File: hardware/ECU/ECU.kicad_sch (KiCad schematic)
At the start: 75 parts, among them IC1 IR4427SPBF, IC2 EL357NB_TA_-G, IC3 EL357NB_TA_-G, J1 USB_B_Micro, J2 TFP09-2-12B, J3 Connector, Q1 S8050, Q2 S8050, Q3 RJP63K2, Q4 RJP63K2, SW1 RESET, SW2 EN, U1 AMS1117-3.3, U2 AMS1117-3.3, U3 CP2102N-Axx-xQFN28, U4 ESP32-WROOM-32U

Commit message: backup
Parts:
- removed C15: 22u, Capacitor_SMD:C_0603_1608Metric_Pad1.08x0.95mm_HandSolder, symbol Device:C
- removed C21, C22, C23: 1n, Capacitor_SMD:C_0603_1608Metric_Pad1.08x0.95mm_HandSolder, symbol Device:C
- removed C8: 22u, Capacitor_SMD:C_0805_2012Metric_Pad1.18x1.45mm_HandSolder, symbol Device:C
- removed C9: 100n, Capacitor_SMD:C_0603_1608Metric_Pad1.08x0.95mm_HandSolder, symbol Device:C
- removed D10: 1n4007, Diode_SMD:D_SMA, symbol Device:D
- removed D11, D3, D8: LED, LED_SMD:LED_0603_1608Metric_Pad1.05x0.95mm_HandSolder, symbol Device:LED
- removed D4: 3.6v, Diode_SMD:D_1206_3216Metric_Pad1.42x1.75mm_HandSolder, symbol Device:D_Zener
- removed D5: 1n4001, Diode_SMD:D_SMA, symbol Device:D
- removed D6, D7: 5v, Diode_SMD:D_SOD-523, symbol Device:D_Zener
- removed J1: USB_B_Micro, Connector_USB:USB_Micro-B_Molex-105017-0001, symbol Connector:USB_B_Micro
- removed J3: Connector, Connector_PinHeader_2.54mm:PinHeader_2x06_P2.54mm_Vertical, symbol Connector:Conn_01x12_Pin
- removed Q1, Q2: S8050, Package_TO_SOT_SMD:SOT-23, symbol Transistor_BJT:S8050
- removed U1: AMS1117-3.3, Package_TO_SOT_SMD:SOT-223-3_TabPin2, symbol Regulator_Linear:AMS1117-3.3
- removed U3: CP2102N-Axx-xQFN28, Package_DFN_QFN:QFN-28-1EP_5x5mm_P0.5mm_EP3.35x3.35mm, symbol Interface_USB:CP2102N-Axx-xQFN28
- removed U4: ESP32-WROOM-32U, RF_Module:ESP32-WROOM-32U, symbol RF_Module:ESP32-WROOM-32U
- added C8: 100u, Capacitor_SMD:CP_Elec_10x10, symbol Device:C_Polarized
- added C9: 1n, Capacitor_SMD:CP_Elec_10x10, symbol Device:C_Polarized
- added D3, D6: ss36, Diode_SMD:D_SMC, symbol Device:D_Schottky
- added D4: m7, Diode_SMD:D_SMA, symbol Device:D
- added D5: LED, LED_SMD:LED_0603_1608Metric_Pad1.05x0.95mm_HandSolder, symbol Device:LED
- added IC4: ESP32-S3-WROOM-1U-N8R8, ESP32S3WROOM1UN8R8, symbol My_Library:ESP32-S3-WROOM-1U-N8R8
- added JP1: BOOT, Connector_PinHeader_2.54mm:PinHeader_1x02_P2.54mm_Vertical, symbol Jumper:Jumper_2_Open
- added JP2: ADDR, Connector_PinHeader_2.54mm:PinHeader_1x03_P2.54mm_Vertical, symbol Jumper:Jumper_3_Open
- added L1: 100u, My_Lirbrary:INDPM102100X400N, symbol Device:L
- added R26, R32, R34, R35, R36, R37: 10k, Resistor_SMD:R_0603_1608Metric_Pad0.98x0.95mm_HandSolder, symbol Device:R
- added R27, R28, R29, R30, R31: 1k, Resistor_SMD:R_0603_1608Metric_Pad0.98x0.95mm_HandSolder, symbol Device:R
- added R33: 100, Resistor_SMD:R_0603_1608Metric_Pad0.98x0.95mm_HandSolder, symbol Device:R
- added U1: LM2576S-5, Package_TO_SOT_SMD:TO-263-5_TabPin3, symbol Regulator_Switching:LM2576S-5
- added U3: LM75A, symbol Sensor_Temperature:LM75B
- added U4: ADS1115IDGS, Package_SO:TSSOP-10_3x3mm_P0.5mm, symbol Analog_ADC:ADS1115IDGS
- C10: value 10u -> 100n; footprint Capacitor_SMD:C_0603_1608Metric_Pad1.08x0.95mm_HandSolder -> Capacitor_SMD:C_0805_2012Metric_Pad1.18x1.45mm_HandSolder
- C11, C14: footprint Capacitor_SMD:C_0603_1608Metric_Pad1.08x0.95mm_HandSolder -> Capacitor_SMD:C_0603_1608Metric
- C12: value 10u -> 100n; footprint Capacitor_SMD:C_0603_1608Metric_Pad1.08x0.95mm_HandSolder -> Capacitor_SMD:C_0603_1608Metric
- C13: value 1n -> 100n; footprint Capacitor_SMD:C_0603_1608Metric_Pad1.08x0.95mm_HandSolder -> Capacitor_SMD:C_0603_1608Metric
- C3, C4: footprint Capacitor_SMD:C_0805_2012Metric_Pad1.18x1.45mm_HandSolder -> Capacitor_SMD:C_0603_1608Metric
- C5: value 100n -> 1u; footprint Capacitor_SMD:C_0805_2012Metric_Pad1.18x1.45mm_HandSolder -> Capacitor_SMD:C_0603_1608Metric
- R1: value 1M -> 10k
- R22, R23: value 470 -> 10k
- R24: value 5k -> 10k
- R25: value 1k -> 10k
- R3, R9: value 2k -> 10k
- R4, R5, R8: value 12k -> 10k
- R6, R7: value 0 -> 10k
- SW1: value RESET -> RESET BTN; footprint Button_Switch_SMD:SW_Push_1P1T_NO_CK_KMR2 -> Button_Switch_SMD:SW_SPST_PTS810
- SW2: value EN -> ZERO BTN; footprint Button_Switch_SMD:SW_Push_1P1T_NO_CK_KMR2 -> Button_Switch_SMD:SW_SPST_PTS810
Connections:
- net RXD is gone; now on net +3.3V: R6.2
- net TXD is gone; now on net +3.3V: R7.2
- net VBUS is gone; now on net GND: C10.1, C3.1, C4.1, R3.1
- net +12V: now also C8.1, U1.1 (VIN); no longer C2.1, C7.1, R2.1, U2.3 (VI)
- net +3.3V: now also C10.2, C13.2, C3.2, C4.2, R23.1, R24.1, R25.2, R4.2, R5.2, IC4.2 (3V3), JP2.1 (A), R26.2, R29.2, R30.2, R32.1, R34.1, R36.1, R37.1, U3.8 (+Vs), U4.8 (VDD); no longer C11.1, C12.1, C14.2, C5.1, R24.2, R8.2
- net COIL_PIN: now also IC2.1 (A), IC4.38 (IO2); no longer IC3.1 (A)
- net FUEL: now also D6.1 (K)
- net FUEL_PIN: now also IC3.1 (A), IC4.39 (IO1); no longer IC2.1 (A)
- net GND: now also C11.1, C12.1, C13.1, C5.1, R1.1, R22.2, R8.1, C8.2, C9.2, D3.2 (A), D6.2 (A), IC4.1 (GND_1), IC4.40 (GND_2), IC4.41 (GND_3), IC4.42 (GND_4), IC4.43 (GND_5), IC4.44 (GND_6), IC4.45 (GND_7), IC4.46 (GND_8), IC4.47 (GND_9), IC4.48 (GND_10), IC4.49 (GND_11), JP1.2 (B), JP2.3 (B), R31.1, U1.3 (GND), U1.5 (~{ON}/OFF), U3.4 (GND), U4.3 (GND); no longer C10.2, C11.2, C12.2, C13.2, C3.2, C4.2, C5.2, R1.2, R25.1
- net O2: now also R33.1
- net at R3.2: now also IC1.4 (INB), IC3.3 (E)
- net at R22.1: now also IC4.16 (IO46); no longer SW1.2
- net at R7.1: now also IC4.15 (IO3)
- net SCL_0: now reaches R5.1
- net SCL_0: now also IC4.7 (IO7), U4.10 (SCL)
- net at R9.2: now also U3.5 (A2)
- net at SW2.2: now also C12.2, R28.2; no longer R23.1
- net at IC1.2 (INA), IC2.3 (E): now also R1.2
- net RESET_PIN: now reaches R6.1
- net RESET_PIN: now also C5.2, IC4.3 (EN), R27.1, R29.1
- net SDA_0: now reaches R4.1
- net SDA_0: now also IC4.6 (IO6), U4.9 (SDA)
- net COIL_IGBT: no longer names the net of IC1.5 (OUT_B)
- net COIL_IGBT: now also R15.2; no longer R11.2
- removed net EN: C13.1, R23.2, R8.1
- net FUEL_IGBT: no longer names the net of IC1.7 (OUT_A)
- net FUEL_IGBT: now also R11.2; no longer R15.2
- removed net IO0: R22.2, R24.1
- new net: D3.1 (K), L1.1, U1.2 (OUT)
- new net: C9.1, D4.2 (A), L1.2, U1.4 (FB)
- new net: IC4.26 (IO45), R8.2
- new net: IC4.27 (IO0), JP1.1 (A)
- new net: R35.1, U4.1 (ADDR)
- new net: JP2.2 (C), R35.2
- new net: R37.2, U4.6 (AIN2)
- new net: C11.2, R27.2, SW1.2
- new net: R23.2, U3.6 (A1)
- new net: D5.1 (K), R31.2
- new net: R24.2, U3.7 (A0)
- new net: R36.2, U4.5 (AIN1)
- new net: C14.2, R33.2, U4.7 (AIN3)
- new net: R34.2, U4.4 (AIN0)
- new net: R32.2, U4.2 (ALERT/RDY)
- new net +5V: C2.1, C7.1, D4.1 (K), R2.1, U2.3 (VI)
- new net CAPTURE_PIN: IC4.10 (IO17)
- new net FSPI_CLK: IC4.20 (IO12)
- new net FSPI_CS: IC4.18 (IO10)
- new net FSPI_MISO: IC4.21 (IO13)
- new net FSPI_MOSI: IC4.19 (IO11)
- new net FUEL_PUMP_PIN: IC4.31 (IO38)
- new net LED_PIN: D5.2 (A), IC4.9 (IO16)
- new net O2_HEATER_PIN: IC4.30 (IO37)
- new net SCL_1: IC4.17 (IO9), R26.1, U3.2 (SCL)
- new net SDA_1: IC4.12 (IO8), R25.1, U3.1 (SDA)
- new net USB_D+: IC4.14 (IO20)
- new net USB_D-: IC4.13 (IO19)
- new net ZERO_PIN: IC4.11 (IO18), R28.1, R30.1
- no-connect marks 42 -> 22
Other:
- note added: "Control"
- note added: "ECU Temp Sensor"
- note added: "MCU"
- note added: "O2_READER"
- note added: "POWER REGULATION"
- note removed: "Battery Regulator"
- note removed: "Buttons"
- note removed: "Connector"
- note removed: "ESP32"
- note removed: "GATE DRIVER"
- note removed: "Power LED"
- note removed: "USB Regulator"
- note removed: "USB to UART"
- moved on the sheet: C1, C16, C17, C18, C19, C2, C20, C6, C7, D1, D2, D9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

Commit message: ECU hardware v0.2 candidate
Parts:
- removed D4: m7, Diode_SMD:D_SMA, symbol Device:D
- removed JP2: ADDR, Connector_PinHeader_2.54mm:PinHeader_1x03_P2.54mm_Vertical, symbol Jumper:Jumper_3_Open
- removed R29: 1k, Resistor_SMD:R_0603_1608Metric_Pad0.98x0.95mm_HandSolder, symbol Device:R
- removed U3: LM75A, symbol Sensor_Temperature:LM75B
- added C21, C24, C25, C26, C27, C28, C29: 100n, Capacitor_SMD:C_0603_1608Metric, symbol Device:C
- added D10, D7: m7, Diode_SMD:D_SMA, symbol Device:D
- added D4: 5v, Diode_SMD:D_1206_3216Metric_Pad1.42x1.75mm_HandSolder, symbol Device:D_Zener
- added D8: ss36, Diode_SMD:D_SMC, symbol Device:D_Schottky
- added IC5: EL357NB_TA_-G, MyLibrary:EL357NG, symbol My_Library:EL357NB_TA_-G
- added J1: AQS, Connector_JST:JST_XH_B6B-XH-A_1x06_P2.50mm_Vertical, symbol Connector:Conn_01x06_Pin
- added J3: CAM_SENSOR, Connector_JST:JST_XH_B6B-XH-A_1x06_P2.50mm_Vertical, symbol Connector:Conn_01x06_Pin
- added J4: USB_B, Connector_USB:USB_B_TE_5787834_Vertical, symbol Connector:USB_B
- added J5: BATTERY, Connector_Molex:Molex_KK-396_5273-02A_1x02_P3.96mm_Vertical, symbol Connector:Conn_01x02_Pin
- added J6: GATEs, Connector_Molex:Molex_KK-396_5273-06A_1x06_P3.96mm_Vertical, symbol Connector:Conn_01x06_Pin
- added J8: CAPTURE_TRG, Connector_JST:JST_XH_B2B-XH-A_1x02_P2.50mm_Vertical, symbol Connector:Conn_01x02_Pin
- added Q1: RJP63K2, Package_TO_SOT_SMD:TO-263-2, symbol Device:Q_NIGBT_GCE
- added R38: 0, Resistor_SMD:R_0603_1608Metric_Pad0.98x0.95mm_HandSolder, symbol Device:R
- added R39: 100, Resistor_SMD:R_0603_1608Metric_Pad0.98x0.95mm_HandSolder, symbol Device:R
- added R42, R43, R51: 10k, Resistor_SMD:R_0603_1608Metric_Pad0.98x0.95mm_HandSolder, symbol Device:R
- added R45: 0.01, MyLibrary:RESC10052X106N, symbol Device:R
- added R47: 130k, Resistor_SMD:R_0603_1608Metric_Pad0.98x0.95mm_HandSolder, symbol Device:R
- added R50: 5.6k, Resistor_SMD:R_0603_1608Metric_Pad0.98x0.95mm_HandSolder, symbol Device:R
- added R52, R53, R54: 1k, Resistor_SMD:R_0603_1608Metric_Pad0.98x0.95mm_HandSolder, symbol Device:R
- added U5: ADS1115IDGS, Package_SO:TSSOP-10_3x3mm_P0.5mm, symbol Analog_ADC:ADS1115IDGS
- added U6: INA180A3, Package_TO_SOT_SMD:SOT-23-5, symbol Amplifier_Current:INA180A3
- added U7: SRV05-4, Package_TO_SOT_SMD:SOT-23-6, symbol Power_Protection:SRV05-4
- C10: footprint Capacitor_SMD:C_0805_2012Metric_Pad1.18x1.45mm_HandSolder -> Capacitor_SMD:C_0603_1608Metric
- IC1: footprint My_Lirbrary:SOIC127P600X175-8N -> MyLibrary:SOIC127P600X175-8N
- IC2, IC3: footprint SOP254P700X200-4N -> MyLibrary:EL357NG
- IC4: footprint ESP32S3WROOM1UN8R8 -> MyLibrary:ESP32S3WROOM1UN4
- J2: footprint TFP09212B -> MyLibrary:TFP09212B
- L1: footprint My_Lirbrary:INDPM102100X400N -> MyLibrary:INDPM102100X400N
- R16, R17, R18, R19, R20, R21: footprint Resistor_SMD:R_0603_1608Metric_Pad0.98x0.95mm_HandSolder -> Resistor_SMD:R_0603_1608Metric
- R27, R28: value 1k -> 100
- R34, R36, R37, R9: value 10k -> 100
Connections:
- net +3.3V: now also R21.1, R24.2, R4.1, R5.1, C21.2, R43.1, R51.2, R53.2, U5.8 (VDD), U6.5 (V+); no longer R21.2, R23.1, R24.1, R34.1, R36.1, R37.1, R4.2, R5.2, R9.1
- net +5V: now also C9.1, L1.2, U1.4 (FB), D10.2 (A), J1.6 (Pin_6), J3.6 (Pin_6), R54.2; no longer C2.1, C7.1, R2.1, U2.3 (VI)
- net CAPTURE_PIN: now also IC4.24 (IO47), R52.1, R53.1; no longer IC4.10 (IO17)
- net COIL: now also J6.1 (Pin_1)
- net COIL_PIN: now also IC4.4 (IO4); no longer IC4.38 (IO2)
- net FSPI_CLK: now also J3.4 (Pin_4)
- net FSPI_CS: now also J3.2 (Pin_2)
- net FSPI_MISO: now also J3.5 (Pin_5)
- net FSPI_MOSI: now also J3.3 (Pin_3)
- net FUEL: now also D6.2 (A), J6.3 (Pin_3); no longer D6.1 (K)
- net FUEL_PIN: now also IC4.5 (IO5); no longer IC4.39 (IO1)
- net FUEL_PUMP_PIN: now also IC4.6 (IO6), IC5.1 (A); no longer IC4.31 (IO38)
- net GND: now also R23.1, R35.1, R9.1, C21.1, C24.1, C25.1, C26.1, C27.1, C28.1, C29.1, D4.2 (A), J1.1 (Pin_1), J3.1 (Pin_1), J4.4 (GND), J4.5 (Shield), J8.2 (Pin_2), Q1.3 (E), R42.1, R45.1, R50.1, U5.3 (GND), U6.2 (GND), U6.3 (+), U7.2 (VN); no longer D6.2 (A)
- net LED_PIN: now also IC4.25 (IO48); no longer IC4.9 (IO16)
- net SCL_0: now also IC4.8 (IO15), R26.1; no longer IC4.7 (IO7), R5.1
- net SCL_1: now also IC4.38 (IO2), R4.2, U5.10 (SCL); no longer IC4.17 (IO9), R26.1
- net SDA_0: now also IC4.7 (IO7), R25.1; no longer IC4.6 (IO6), R4.1
- net SDA_1: now also IC4.39 (IO1), R5.2, U5.9 (SDA); no longer IC4.12 (IO8), R25.1
- net SD_CLK: now also IC4.34 (IO41)
- net SD_CMD: now also IC4.35 (IO42)
- net SD_DAT0: now also IC4.33 (IO40)
- net USB_D+: now also J4.3 (D+), U7.3 (IO2), U7.4 (IO3)
- net USB_D-: now also J4.2 (D-), U7.1 (IO1), U7.6 (IO4)
- net ZERO_PIN: now also IC4.9 (IO16); no longer IC4.11 (IO18)
- net at R9.2: now also IC5.2 (K)
- net SD_DAT1: now reaches IC4.32 (IO39)
- net SD_DAT1: now also J2.8 (DAT1), R21.2
- net SD_DAT3: now reaches IC4.36 (RXD0)
- net SD_DAT3: now also J2.2 (CD/DAT3), R19.2
- net SD_DAT2: now reaches IC4.37 (TXD0)
- net SD_DAT2: now also J2.1 (DAT2), R20.2
- net at U4.1 (ADDR): now also R35.2; no longer R35.1
- net at R37.2, U4.6 (AIN2): now also C27.2
- net at R23.2: now also IC5.3 (E), R38.2
- net at R36.2, U4.5 (AIN1): now also C28.2
- net at R34.2, U4.4 (AIN0): now also C29.2
- net +12V renamed +BATT
- net +BATT: now also D6.1 (K), D8.1 (K), IC5.4 (C), J5.2 (Pin_2), J6.2 (Pin_2), J6.4 (Pin_4), J6.6 (Pin_6), R47.2
- net O2 renamed AFR
- net AFR: now also J1.5 (Pin_5)
- net O2_HEATER_PIN: no longer names the net of IC4.30 (IO37)
- new net: C25.2, R47.1, R50.2, U5.4 (AIN0)
- new net: C24.2, R39.2, U5.5 (AIN1)
- new net: D7.2 (A), J4.1 (VBUS), U7.5 (VP)
- new net: R24.1, U5.6 (AIN2)
- new net: R43.2, U5.2 (ALERT/RDY)
- new net: C26.2, J8.1 (Pin_1), R52.2
- new net: Q1.1 (G), R38.1
- new net: R42.2, U5.1 (ADDR)
- new net: R51.1, U5.7 (AIN3)
- new net +4V: C2.1, C7.1, D10.1 (K), D4.1 (K), D7.1 (K), R2.1, U2.3 (VI)
- new net -BATT: J5.1 (Pin_1), R45.2, U6.4 (-)
- new net BATT_OUT: R39.1, U6.1
- new net IAT: J1.2 (Pin_2), R34.1, R54.1
- new net MPS: J1.3 (Pin_3), R36.1
- new net PUMP: D8.2 (A), J6.5 (Pin_5), Q1.2 (C)
- new net TPS: J1.4 (Pin_4), R37.1
- no-connect marks 22 -> 14
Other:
- note added: "Air Quality Sensor"
- note added: "Connectors"
- note added: "Power Sense(s)"
- note removed: "ECU Temp Sensor"
- note removed: "O2_READER"
- moved on the sheet: C1, C11, C12, C13, C14, C16, C2, C3, C4, C5, C6, C7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

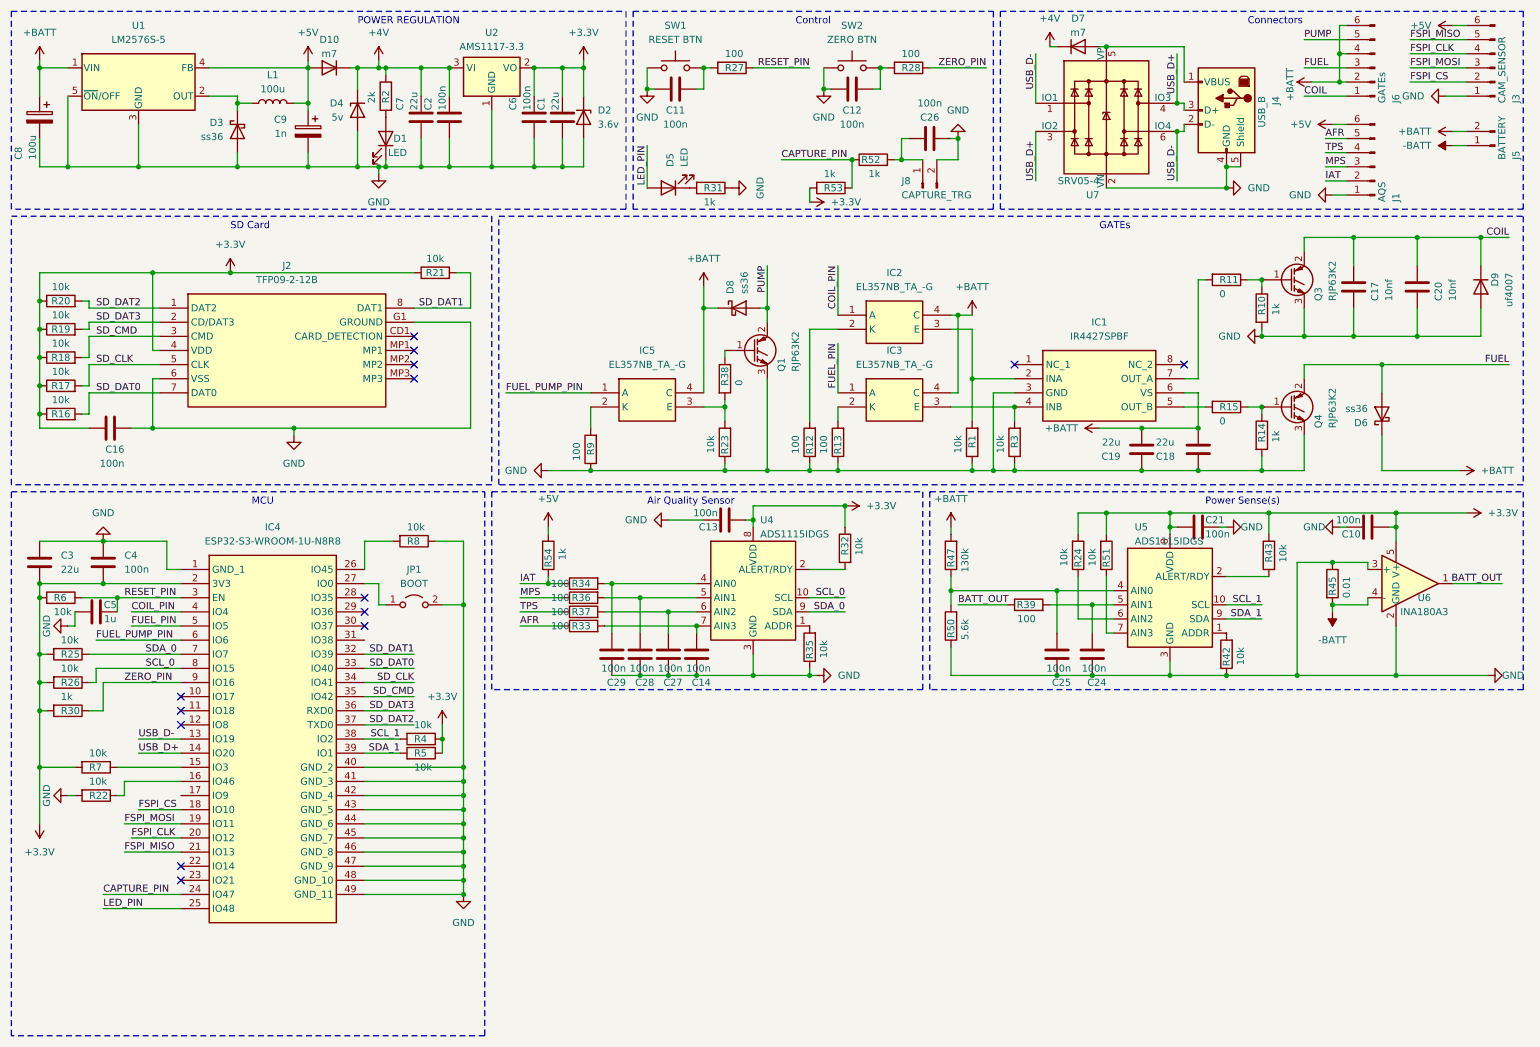
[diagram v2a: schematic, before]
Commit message: add idle control circuit
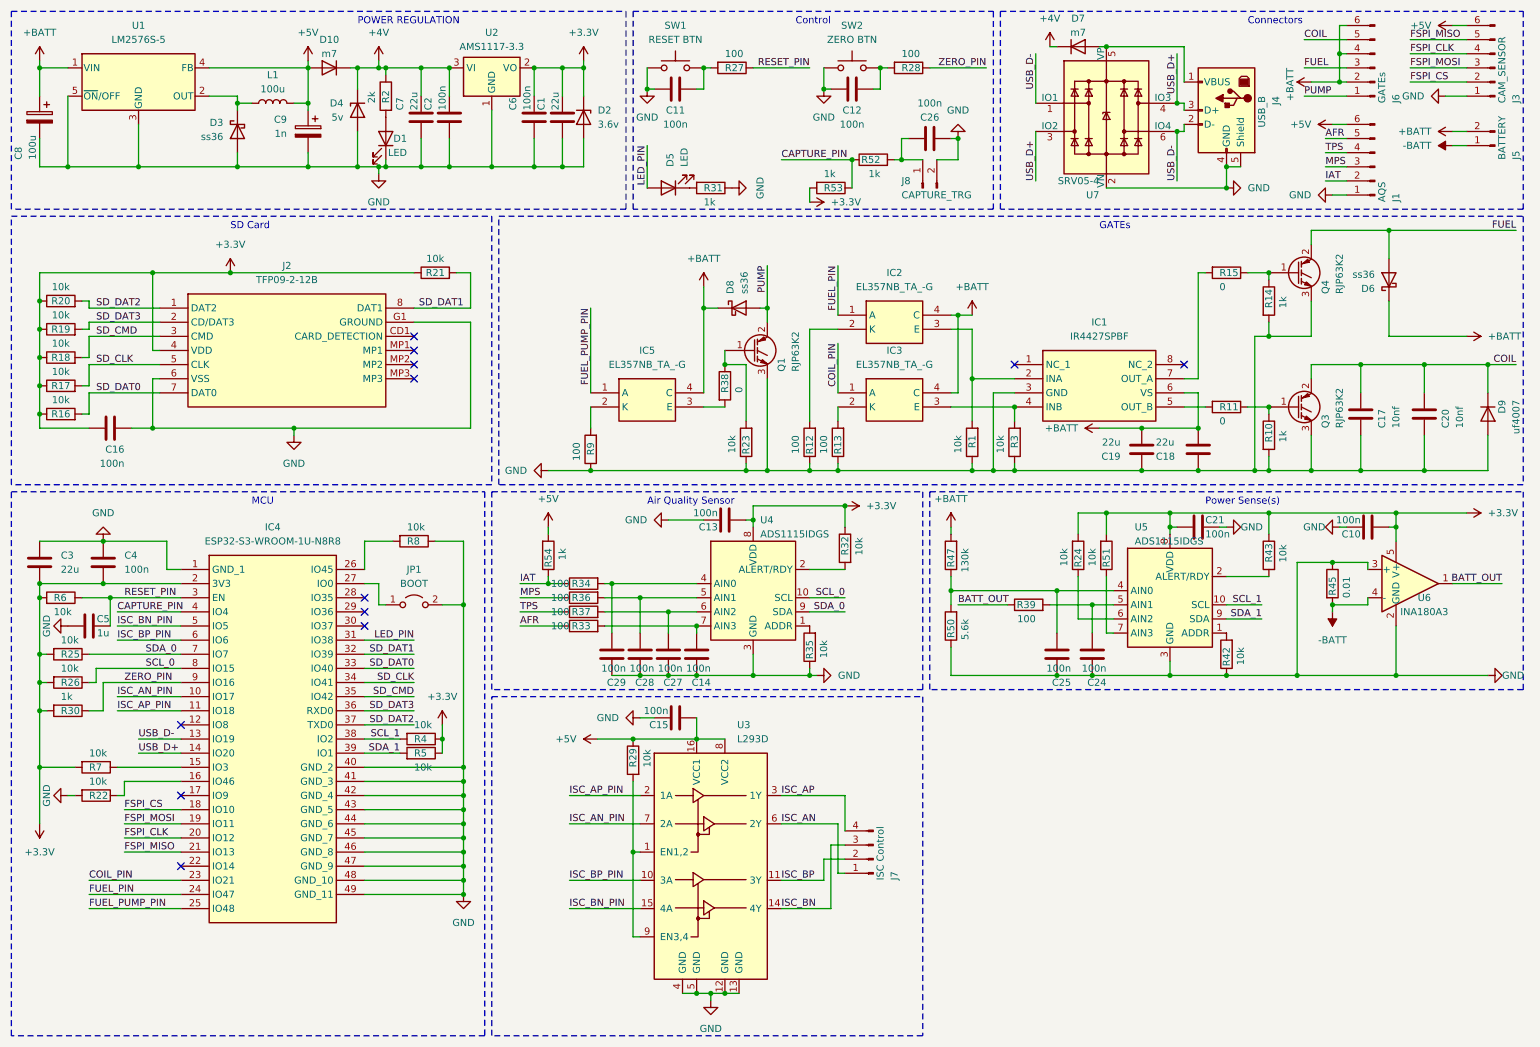
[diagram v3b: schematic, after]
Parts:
- added C15: 100n, Capacitor_SMD:C_0603_1608Metric, symbol Device:C
- added J7: ISC Control, Connector_JST:JST_XH_B4B-XH-A_1x04_P2.50mm_Vertical, symbol Connector:Conn_01x04_Pin
- added R29: 10k, Resistor_SMD:R_0603_1608Metric_Pad0.98x0.95mm_HandSolder, symbol Device:R
- added U3: L293D, Package_DIP:DIP-16_W7.62mm_SMDSocket_SmallPads, symbol Driver_Motor:L293D
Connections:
- net +5V: now also C15.2, R29.1, U3.16 (VCC1), U3.8 (VCC2)
- net CAPTURE_PIN: now also IC4.4 (IO4); no longer IC4.24 (IO47)
- net COIL: now also J6.5 (Pin_5); no longer J6.1 (Pin_1)
- net COIL_PIN: now also IC3.1 (A), IC4.23 (IO21); no longer IC2.1 (A), IC4.4 (IO4)
- net FUEL_PIN: now also IC2.1 (A), IC4.24 (IO47); no longer IC3.1 (A), IC4.5 (IO5)
- net FUEL_PUMP_PIN: now also IC4.25 (IO48); no longer IC4.6 (IO6)
- net GND: now also C15.1, U3.12 (GND), U3.13 (GND), U3.4 (GND), U3.5 (GND)
- net LED_PIN: now also IC4.31 (IO38); no longer IC4.25 (IO48)
- net PUMP: now also J6.1 (Pin_1); no longer J6.5 (Pin_5)
- net ISC_AN_PIN: now reaches IC4.10 (IO17)
- net ISC_AN_PIN: now also U3.7 (2A)
- net ISC_AP_PIN: now reaches IC4.11 (IO18)
- net ISC_AP_PIN: now also U3.2 (1A)
- net at R15.2: now also IC1.7 (OUT_A); no longer IC1.5 (OUT_B)
- net at R11.2: now also IC1.5 (OUT_B); no longer IC1.7 (OUT_A)
- net at IC5.3 (E), R38.2: no longer R23.2
- net at Q1.1 (G), R38.1: now also R23.2
- new net: R29.2, U3.1 (EN1,2), U3.9 (EN3,4)
- new net ISC_AN: J7.1 (Pin_1), U3.6 (2Y)
- new net ISC_AP: J7.4 (Pin_4), U3.3 (1Y)
- new net ISC_BN: J7.3 (Pin_3), U3.14 (4Y)
- new net ISC_BN_PIN: IC4.5 (IO5), U3.15 (4A)
- new net ISC_BP: J7.2 (Pin_2), U3.11 (3Y)
- new net ISC_BP_PIN: IC4.6 (IO6), U3.10 (3A)
- no-connect marks 14 -> 12
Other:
- moved on the sheet: C17, C20, C5, D6, D9, Q3, Q4, R10, R11, R14, R15, R23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
